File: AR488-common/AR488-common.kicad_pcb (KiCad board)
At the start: 2 copper layers, 63.5 x 40.6 mm, 9 parts, among them J1 GPIB-24, J2 Conn_02x12_Odd_Even, J3 Barrel_Jack, J4 Screw_Terminal_01x02, U1 SN75160BDW, U2 SN75162BDW

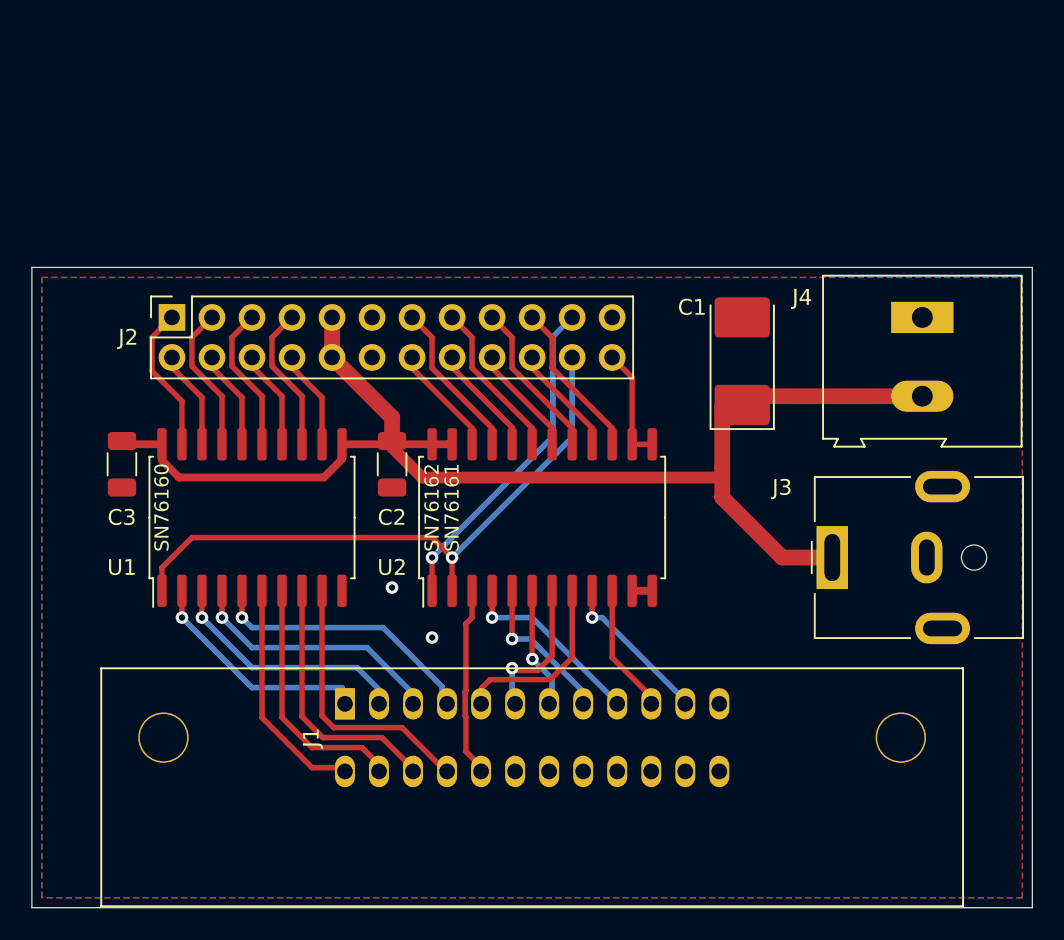
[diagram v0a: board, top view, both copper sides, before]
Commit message: Finish the commons board + esp32 s2 soala + esp32 devkitc boards
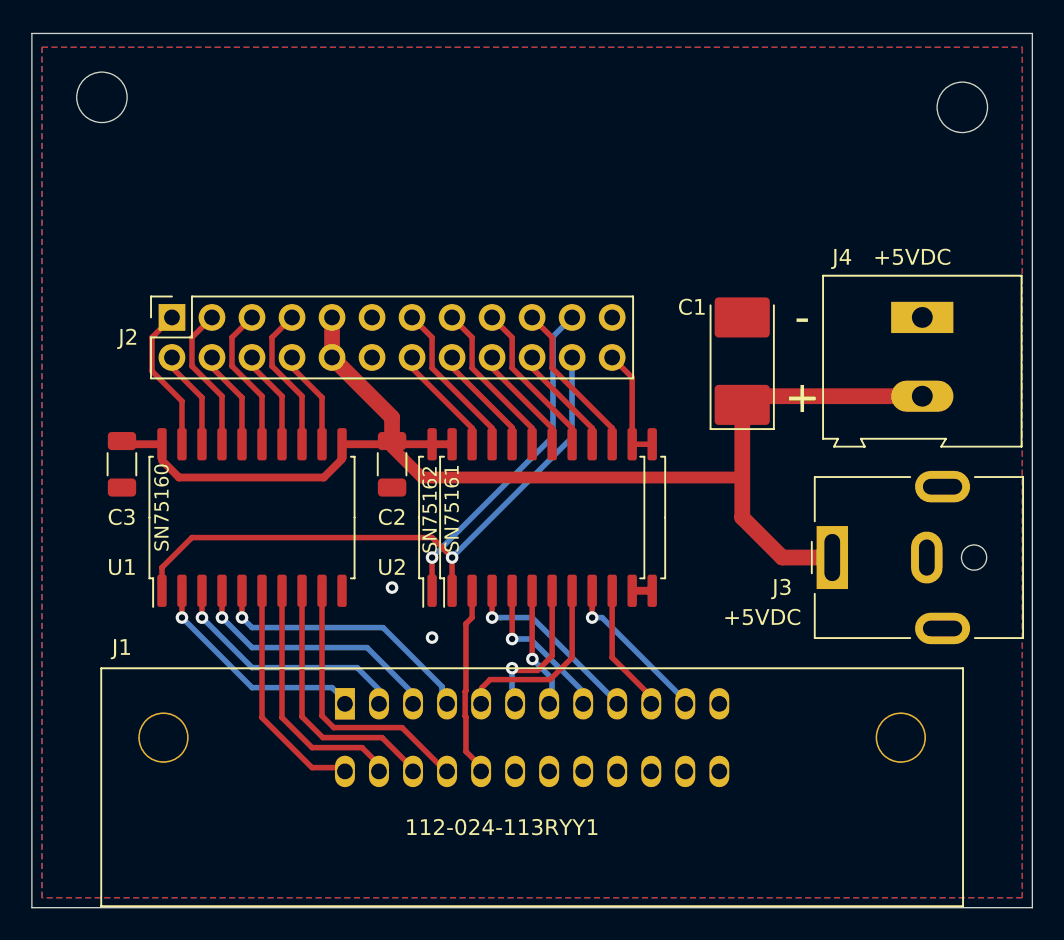
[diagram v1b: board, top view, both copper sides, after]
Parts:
- added REF**: MountingHole_3.2mm_M3_ISO7380, MountingHole:MountingHole_3.2mm_M3_ISO7380, F.Cu at (211.5, 59.7)
- added REF**: MountingHole_3.2mm_M3_ISO7380, MountingHole:MountingHole_3.2mm_M3_ISO7380, F.Cu at (156.8, 59.1)
- J1: value GPIB-24 -> NorComp - 112-024-113RYY1
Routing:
- net +5V: track 83.7 -> 84.3 mm
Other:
- board size 63.5 x 40.6 mm -> 63.5 x 55.5 mm
- board text added: "+"
- board text added: "+5VDC"
- board text added: "+5v"
- board text added: "-"
- board text added: "112-024-113RYY1"
- board text added: "AR488-GPIB SN7516x - IEEE488 board https://whatever.sdfa.org/gpib"
- board text added: "ATN"
- board text added: "CC BY-SA 3.0 David Douard <david.douard@sdfa3.org>"
- board text added: "D1"
- board text added: "D2"
- board text added: "D3"
- board text added: "D4"
- board text added: "D5"
- board text added: "D6"
- board text added: "D7"
- board text added: "D8"
- board text added: "DAV"
- board text added: "DC"
- board text added: "EOI"
- board text added: "GND"
- board text added: "IFC"
- board text added: "NDAC"
- board text added: "NRFD"
- board text added: "REN"
- board text added: "SC"
- board text added: "SN75160"
- board text added: "SN75162"
- board text added: "SRQ"
- board text added: "TE"
- board text removed: "SN76160"
- board text removed: "SN76161"
- board text removed: "SN76162"

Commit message: Several minor fixes and adjustments in PCBs
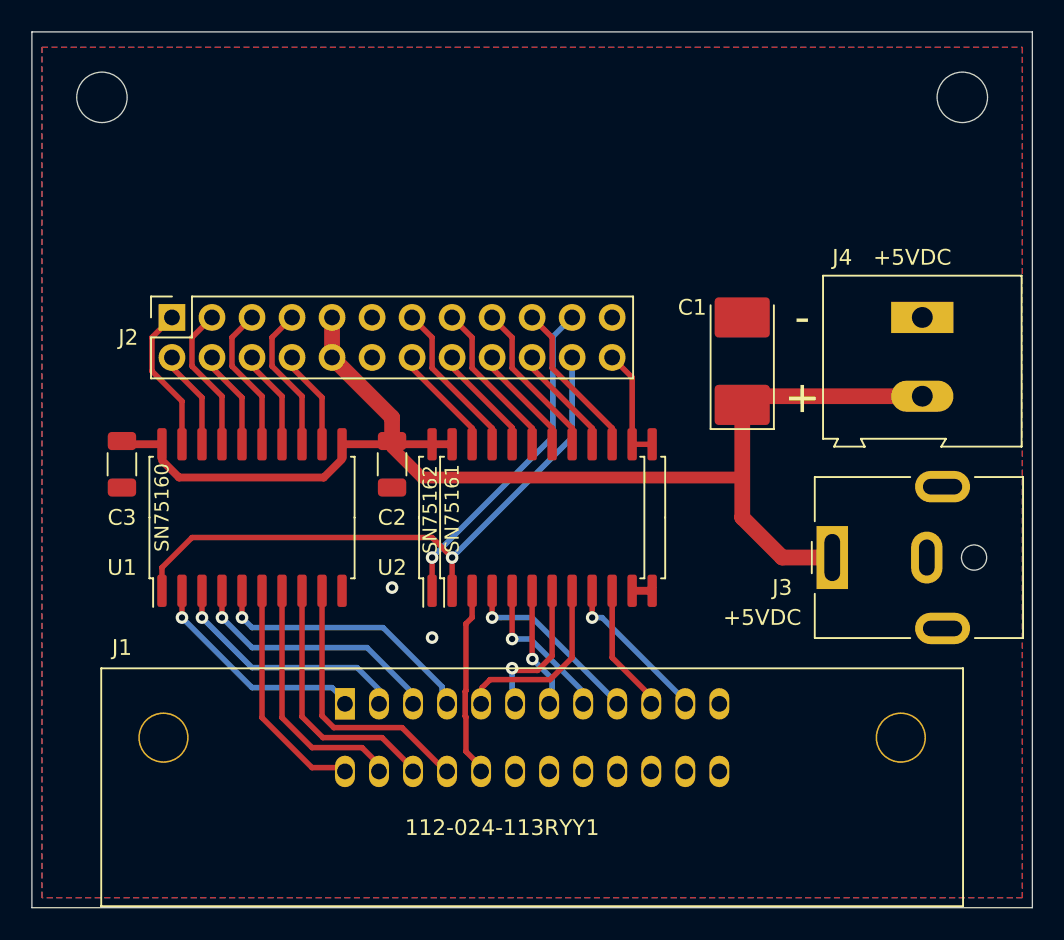
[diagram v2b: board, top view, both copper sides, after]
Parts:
- moved REF** 0.63 mm to (211.5, 59.1)
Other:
- board size 63.5 x 55.5 mm -> 63.5 x 55.6 mm
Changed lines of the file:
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@@
   (general
     (thickness 1.6)
-    (drawings 60)
+    (drawings 62)
     (tracks 180)
     (zones 0)
@@
   )
   (module MountingHole:MountingHole_3.2mm_M3_ISO7380 (layer F.Cu)
-    (at 211.455 59.69)
+    (at 211.455 59.055)
     (descr "Mounting Hole 3.2mm, no annular, M3, ISO7380")
     (tags "mounting hole 3.2mm no annular m3 iso7380")
@@
       (effects (font (size 1 1) (thickness 0.15)))
     )
-    (fp_text user %R (at 0.3 0) (layer F.Fab)
-      (effects (font (size 1 1) (thickness 0.15)))
-    )
     (fp_circle (center 0 0) (end 2.85 0) (layer Cmts.User) (width 0.15))
     (fp_circle (center 0 0) (end 3.1 0) (layer F.CrtYd) (width 0.05))
-    (pad 1 np_thru_hole circle (at 0 0) (size 3.2 3.2) (drill 3.2) (layers *.Cu *.Mask))
+    (fp_text user %R (at 0.3 0) (layer F.Fab) hide
+      (effects (font (size 1 1) (thickness 0.15)))
+    )
+    (pad "" np_thru_hole circle (at 0 0) (size 3.2 3.2) (drill 3.2) (layers *.Cu *.Mask))
   )
   (module MountingHole:MountingHole_3.2mm_M3_ISO7380 (layer F.Cu)
@@
       (effects (font (size 1 1) (thickness 0.15)))
     )
-    (fp_text user %R (at 0.3 0) (layer F.Fab)
-      (effects (font (size 1 1) (thickness 0.15)))
-    )
     (fp_circle (center 0 0) (end 2.85 0) (layer Cmts.User) (width 0.15))
     (fp_circle (center 0 0) (end 3.1 0) (layer F.CrtYd) (width 0.05))
+    (fp_text user %R (at 6.731 -1.016) (layer F.Fab) hide
+      (effects (font (size 1 1) (thickness 0.15)))
+    )
     (pad 1 np_thru_hole circle (at 0 0) (size 3.2 3.2) (drill 3.2) (layers *.Cu *.Mask))
   )
@@
     )
   )
+  (dimension 0.5334 (width 0.15) (layer Dwgs.User)
+    (gr_text "0.533 mm" (at 161.0233 96.49) (layer Dwgs.User)
+      (effects (font (size 1 1) (thickness 0.15)))
+    )
+    (feature1 (pts (xy 161.29 99.695) (xy 161.29 97.203579)))
+    (feature2 (pts (xy 160.7566 99.695) (xy 160.7566 97.203579)))
+    (crossbar (pts (xy 160.7566 97.79) (xy 161.29 97.79)))
+    (arrow1a (pts (xy 161.29 97.79) (xy 160.163496 98.376421)))
+    (arrow1b (pts (xy 161.29 97.79) (xy 160.163496 97.203579)))
+    (arrow2a (pts (xy 160.7566 97.79) (xy 161.883104 98.376421)))
+    (arrow2b (pts (xy 160.7566 97.79) (xy 161.883104 97.203579)))
+  )
+  (dimension 4.153 (width 0.15) (layer Dwgs.User)
+    (gr_text "4.153 mm" (at 146.655 56.9785 270) (layer Dwgs.User)
+      (effects (font (size 1 1) (thickness 0.15)))
+    )
+    (feature1 (pts (xy 152.4 59.055) (xy 147.368579 59.055)))
+    (feature2 (pts (xy 152.4 54.902) (xy 147.368579 54.902)))
+    (crossbar (pts (xy 147.955 54.902) (xy 147.955 59.055)))
+    (arrow1a (pts (xy 147.955 59.055) (xy 147.368579 57.928496)))
+    (arrow1b (pts (xy 147.955 59.055) (xy 148.541421 57.928496)))
+    (arrow2a (pts (xy 147.955 54.902) (xy 147.368579 56.028504)))
+    (arrow2b (pts (xy 147.955 54.902) (xy 148.541421 56.028504)))
+  )
+  (dimension 4.445 (width 0.15) (layer Dwgs.User)
+    (gr_text "4.445 mm" (at 154.6225 41.88) (layer Dwgs.User)
+      (effects (font (size 1 1) (thickness 0.15)))
+    )
+    (feature1 (pts (xy 156.845 55) (xy 156.845 42.593579)))
+    (feature2 (pts (xy 152.4 55) (xy 152.4 42.593579)))
+    (crossbar (pts (xy 152.4 43.18) (xy 156.845 43.18)))
+    (arrow1a (pts (xy 156.845 43.18) (xy 155.718496 43.766421)))
+    (arrow1b (pts (xy 156.845 43.18) (xy 155.718496 42.593579)))
+    (arrow2a (pts (xy 152.4 43.18) (xy 153.526504 43.766421)))
+    (arrow2b (pts (xy 152.4 43.18) (xy 153.526504 42.593579)))
+  )
   (gr_text 112-024-113RYY1 (at 182.245 105.41) (layer F.SilkS)
     (effects (font (size 1 1) (thickness 0.15)))
@@
     (arrow2a (pts (xy 152.4 50.8) (xy 153.526504 51.386421)))
     (arrow2b (pts (xy 152.4 50.8) (xy 153.526504 50.213579)))
-  )
-  (dimension 55.49 (width 0.15) (layer Dwgs.User)
-    (gr_text "55.490 mm" (at 146.655 82.745 270) (layer Dwgs.User)
-      (effects (font (size 1 1) (thickness 0.15)))
-    )
-    (feature1 (pts (xy 152.4 110.49) (xy 147.368579 110.49)))
-    (feature2 (pts (xy 152.4 55) (xy 147.368579 55)))
-    (crossbar (pts (xy 147.955 55) (xy 147.955 110.49)))
-    (arrow1a (pts (xy 147.955 110.49) (xy 147.368579 109.363496)))
-    (arrow1b (pts (xy 147.955 110.49) (xy 148.541421 109.363496)))
-    (arrow2a (pts (xy 147.955 55) (xy 147.368579 56.126504)))
-    (arrow2b (pts (xy 147.955 55) (xy 148.541421 56.126504)))
   )
   (target plus (at 207.5434 99.695) (size 5) (width 0.05) (layer Edge.Cuts))
@@
   (gr_line (start 178.435 80.01) (end 178.435 91.44) (layer F.CrtYd) (width 0.05))
   (gr_line (start 215.9 110.49) (end 152.4 110.49) (layer Edge.Cuts) (width 0.05))
-  (gr_line (start 215.9 55) (end 215.9 110.49) (layer Edge.Cuts) (width 0.05))
-  (gr_line (start 152.4 55) (end 215.9 55) (layer Edge.Cuts) (width 0.05))
-  (gr_line (start 152.4 110.49) (end 152.4 55) (layer Edge.Cuts) (width 0.05))
+  (gr_line (start 215.9 54.902) (end 215.9 110.49) (layer Edge.Cuts) (width 0.05))
+  (gr_line (start 152.4 54.902) (end 215.9 54.902) (layer Edge.Cuts) (width 0.05))
+  (gr_line (start 152.4 110.49) (end 152.4 54.902) (layer Edge.Cuts) (width 0.05))
   (via (at 175.26 90.17) (size 0.8) (drill 0.4) (layers F.Cu B.Cu) (net 1))
   (via (at 177.8 93.345) (size 0.8) (drill 0.4) (layers F.Cu B.Cu) (net 1))
